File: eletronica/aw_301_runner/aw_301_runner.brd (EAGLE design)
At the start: 50.5 x 50.8 mm, 6 parts, among them IC1 ATTINY2313V

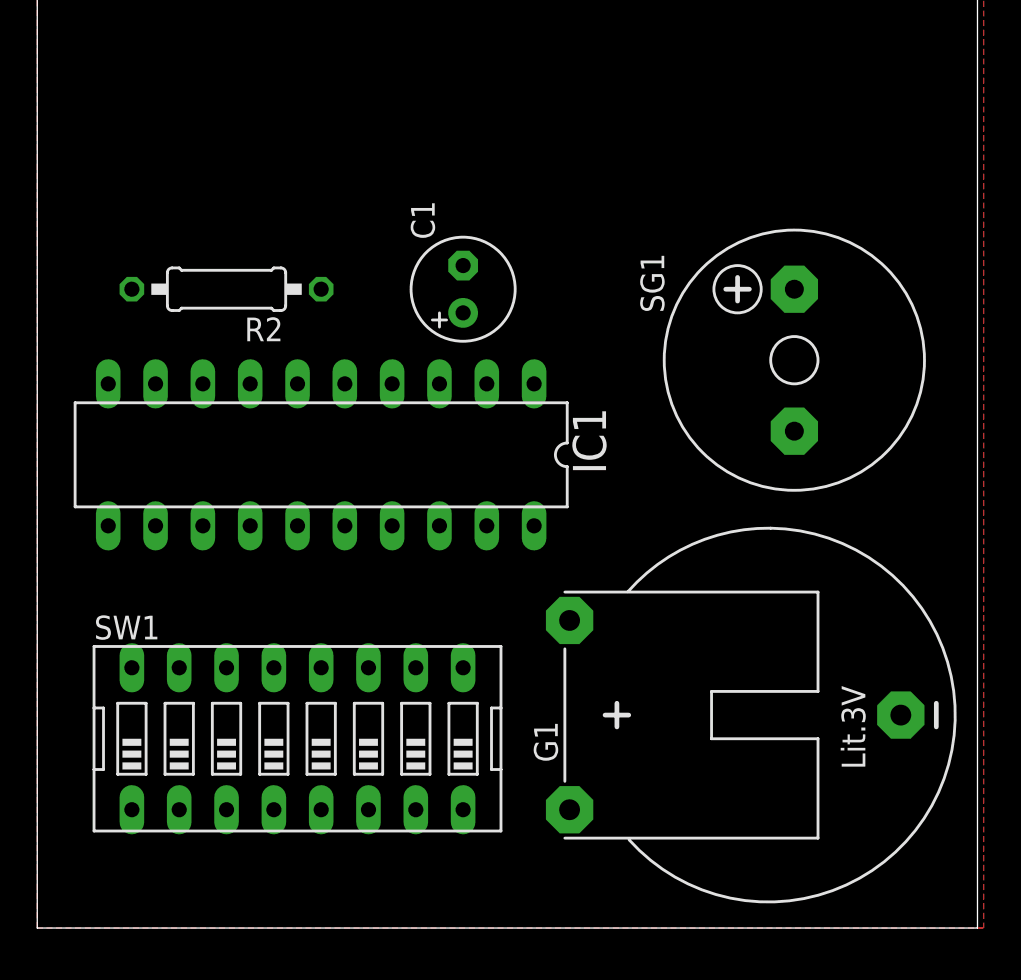
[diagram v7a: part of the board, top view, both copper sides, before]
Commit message: 
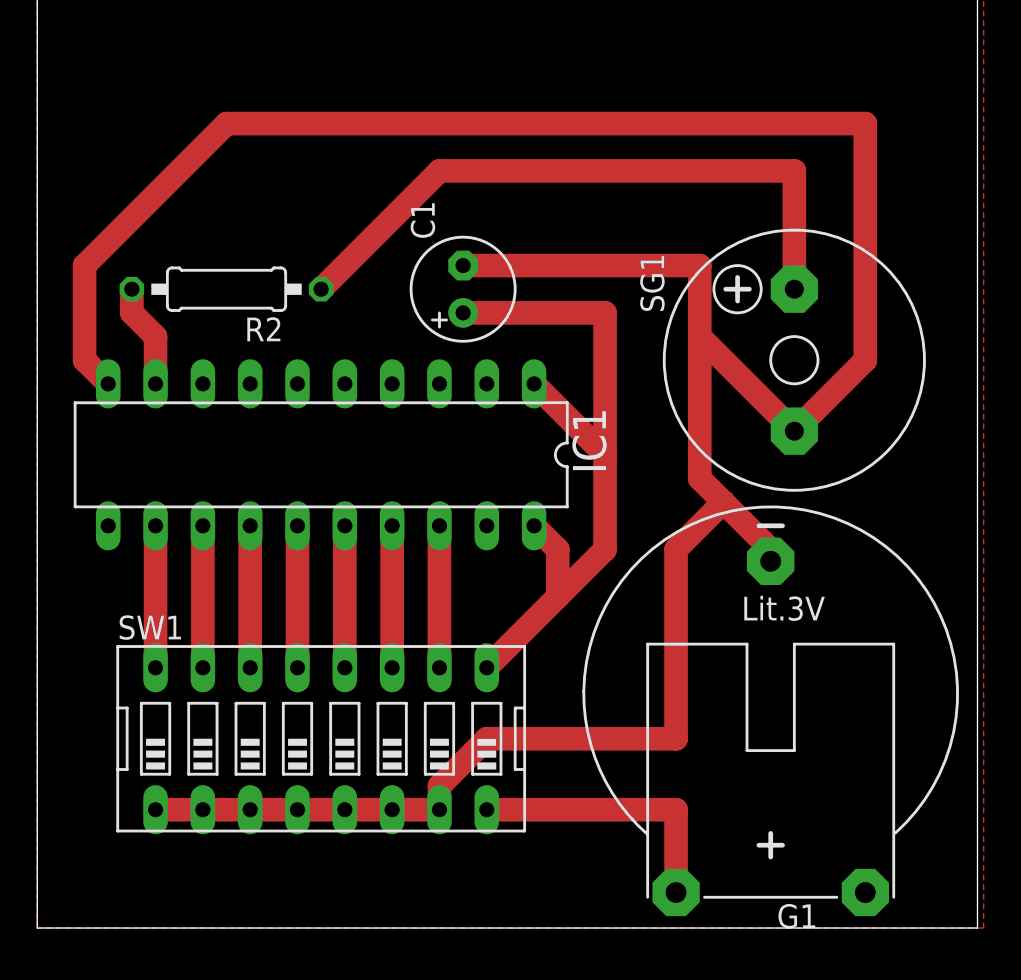
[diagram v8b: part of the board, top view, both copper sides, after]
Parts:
- moved G1 1.27 mm to (39.4, 12.7), turned to 180 degrees
- moved SW1 1.27 mm to (15.2, 10.2)
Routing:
- net GND: track 0.00 -> 151.4 mm
- net N$5: track 0.00 -> 39.0 mm
- net N$3: track 0.00 -> 34.4 mm
- net VCC: track 0.00 -> 14.6 mm
- net N$9: track 0.00 -> 7.62 mm
- net N$8: track 0.00 -> 7.62 mm
- net N$7: track 0.00 -> 7.62 mm
- net N$4: track 0.00 -> 7.62 mm
- net N$12: track 0.00 -> 7.62 mm
- net N$11: track 0.00 -> 7.62 mm
- net N$10: track 0.00 -> 7.62 mm
- net N$2: track 0.00 -> 5.61 mm
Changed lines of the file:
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@@
 <param name="PrefDir.14" value="0"/>
 <param name="PrefDir.15" value="0"/>
-<param name="PrefDir.16" value="-"/>
+<param name="PrefDir.16" value="0"/>
 <param name="cfVia" value="8"/>
 <param name="cfNonPref" value="5"/>
@@
 <attribute name="OC_FARNELL" value="unknown" x="-11.43" y="68.58" size="1.778" layer="27" rot="R180" display="off"/>
 </element>
-<element name="SW1" library="special" package="EDG-08" value="" x="13.97" y="10.16"/>
-<element name="G1" library="battery" package="CR2032H" value="CR2032H" x="39.37" y="11.43" rot="R90"/>
+<element name="SW1" library="special" package="EDG-08" value="" x="15.24" y="10.16"/>
+<element name="G1" library="battery" package="CR2032H" value="CR2032H" x="39.37" y="12.7" rot="R180"/>
 <element name="C1" library="resistor" package="E2,5-6" value="100mF" x="22.86" y="34.29" rot="R90"/>
 <element name="R2" library="rcl" package="0207/10" value="50" x="10.16" y="34.29" rot="R180"/>
@@
 <contactref element="SW1" pad="6"/>
 <contactref element="SW1" pad="7"/>
-<wire x1="20.32" y1="6.35" x2="46.355" y2="11.43" width="0" layer="19" extent="1-1"/>
-<wire x1="17.78" y1="6.35" x2="20.32" y2="6.35" width="0" layer="19" extent="1-1"/>
-<wire x1="15.24" y1="6.35" x2="17.78" y2="6.35" width="0" layer="19" extent="1-1"/>
-<wire x1="12.7" y1="6.35" x2="15.24" y2="6.35" width="0" layer="19" extent="1-1"/>
-<wire x1="10.16" y1="6.35" x2="12.7" y2="6.35" width="0" layer="19" extent="1-1"/>
-<wire x1="7.62" y1="6.35" x2="10.16" y2="6.35" width="0" layer="19" extent="1-1"/>
-<wire x1="5.08" y1="6.35" x2="7.62" y2="6.35" width="0" layer="19" extent="1-1"/>
-<wire x1="40.64" y1="26.67" x2="5.08" y2="6.35" width="0" layer="19" extent="1-1"/>
-<wire x1="3.81" y1="29.21" x2="5.08" y2="6.35" width="0" layer="19" extent="1-1"/>
-<wire x1="22.86" y1="35.56" x2="3.81" y2="29.21" width="0" layer="19" extent="1-1"/>
+<wire x1="8.89" y1="6.35" x2="6.35" y2="6.35" width="1.27" layer="1"/>
+<wire x1="8.89" y1="6.35" x2="11.43" y2="6.35" width="1.27" layer="1"/>
+<wire x1="11.43" y1="6.35" x2="13.97" y2="6.35" width="1.27" layer="1"/>
+<wire x1="13.97" y1="6.35" x2="16.51" y2="6.35" width="1.27" layer="1"/>
+<wire x1="16.51" y1="6.35" x2="19.05" y2="6.35" width="1.27" layer="1"/>
+<wire x1="19.05" y1="6.35" x2="21.59" y2="6.35" width="1.27" layer="1"/>
+<wire x1="2.54" y1="30.48" x2="3.81" y2="29.21" width="1.27" layer="1"/>
+<wire x1="2.54" y1="35.56" x2="2.54" y2="30.48" width="1.27" layer="1"/>
+<wire x1="10.16" y1="43.18" x2="2.54" y2="35.56" width="1.27" layer="1"/>
+<wire x1="44.45" y1="43.18" x2="10.16" y2="43.18" width="1.27" layer="1"/>
+<wire x1="44.45" y1="30.48" x2="44.45" y2="43.18" width="1.27" layer="1"/>
+<wire x1="40.64" y1="26.67" x2="44.45" y2="30.48" width="1.27" layer="1"/>
+<wire x1="35.56" y1="35.56" x2="22.86" y2="35.56" width="1.27" layer="1"/>
+<wire x1="35.56" y1="31.75" x2="35.56" y2="35.56" width="1.27" layer="1"/>
+<wire x1="40.64" y1="26.67" x2="35.56" y2="31.75" width="1.27" layer="1"/>
+<wire x1="35.56" y1="24.13" x2="36.83" y2="22.86" width="1.27" layer="1"/>
+<wire x1="36.83" y1="22.86" x2="39.37" y2="20.32" width="1.27" layer="1"/>
+<wire x1="35.56" y1="31.75" x2="35.56" y2="24.13" width="1.27" layer="1"/>
+<wire x1="39.37" y1="20.32" x2="39.37" y2="19.685" width="1.27" layer="1"/>
+<wire x1="21.59" y1="7.62" x2="21.59" y2="6.35" width="1.27" layer="1"/>
+<wire x1="24.13" y1="10.16" x2="21.59" y2="7.62" width="1.27" layer="1"/>
+<wire x1="34.29" y1="10.16" x2="24.13" y2="10.16" width="1.27" layer="1"/>
+<wire x1="34.29" y1="20.32" x2="34.29" y2="10.16" width="1.27" layer="1"/>
+<wire x1="36.83" y1="22.86" x2="34.29" y2="20.32" width="1.27" layer="1"/>
 </signal>
 <signal name="N$2">
 <contactref element="IC1" pad="9"/>
 <contactref element="R2" pad="2"/>
-<wire x1="6.35" y1="29.21" x2="5.08" y2="34.29" width="0" layer="19" extent="1-1"/>
+<wire x1="6.35" y1="31.75" x2="6.35" y2="29.21" width="1.27" layer="1"/>
+<wire x1="5.08" y1="33.02" x2="6.35" y2="31.75" width="1.27" layer="1"/>
+<wire x1="5.08" y1="34.29" x2="5.08" y2="33.02" width="1.27" layer="1"/>
 </signal>
 <signal name="N$6">
@@
 <contactref element="R2" pad="1"/>
 <contactref element="SG1" pad="+"/>
-<wire x1="40.64" y1="34.29" x2="15.24" y2="34.29" width="0" layer="19" extent="1-1"/>
+<wire x1="21.59" y1="40.64" x2="15.24" y2="34.29" width="1.27" layer="1"/>
+<wire x1="40.64" y1="40.64" x2="21.59" y2="40.64" width="1.27" layer="1"/>
+<wire x1="40.64" y1="34.29" x2="40.64" y2="40.64" width="1.27" layer="1"/>
 </signal>
 <signal name="VCC">
 <contactref element="G1" pad="+"/>
 <contactref element="SW1" pad="8"/>
-<wire x1="22.86" y1="6.35" x2="28.575" y2="16.51" width="0" layer="19" extent="1-1"/>
+<wire x1="34.29" y1="6.35" x2="24.13" y2="6.35" width="1.27" layer="1"/>
+<wire x1="34.29" y1="1.905" x2="34.29" y2="6.35" width="1.27" layer="1"/>
 </signal>
 <signal name="N$5">
@@
 <contactref element="C1" pad="+"/>
 <contactref element="IC1" pad="1"/>
-<wire x1="26.67" y1="21.59" x2="26.67" y2="29.21" width="0" layer="19" extent="1-1"/>
-<wire x1="22.86" y1="13.97" x2="26.67" y2="21.59" width="0" layer="19" extent="1-1"/>
-<wire x1="22.86" y1="33.02" x2="26.67" y2="29.21" width="0" layer="19" extent="1-1"/>
+<wire x1="27.94" y1="17.78" x2="24.13" y2="13.97" width="1.27" layer="1"/>
+<wire x1="27.94" y1="20.32" x2="27.94" y2="17.78" width="1.27" layer="1"/>
+<wire x1="26.67" y1="21.59" x2="27.94" y2="20.32" width="1.27" layer="1"/>
+<wire x1="30.48" y1="25.4" x2="26.67" y2="29.21" width="1.27" layer="1"/>
+<wire x1="30.48" y1="20.32" x2="30.48" y2="25.4" width="1.27" layer="1"/>
+<wire x1="27.94" y1="17.78" x2="30.48" y2="20.32" width="1.27" layer="1"/>
+<wire x1="30.48" y1="33.02" x2="22.86" y2="33.02" width="1.27" layer="1"/>
+<wire x1="30.48" y1="25.4" x2="30.48" y2="33.02" width="1.27" layer="1"/>
 </signal>
 <signal name="N$4">
 <contactref element="IC1" pad="12"/>
 <contactref element="SW1" pad="16"/>
-<wire x1="5.08" y1="13.97" x2="6.35" y2="21.59" width="0" layer="19" extent="1-1"/>
+<wire x1="6.35" y1="21.59" x2="6.35" y2="13.97" width="1.27" layer="1"/>
 </signal>
 <signal name="N$7">
 <contactref element="IC1" pad="13"/>
 <contactref element="SW1" pad="15"/>
-<wire x1="7.62" y1="13.97" x2="8.89" y2="21.59" width="0" layer="19" extent="1-1"/>
+<wire x1="8.89" y1="21.59" x2="8.89" y2="13.97" width="1.27" layer="1"/>
 </signal>
 <signal name="N$8">
 <contactref element="IC1" pad="14"/>
 <contactref element="SW1" pad="14"/>
-<wire x1="10.16" y1="13.97" x2="11.43" y2="21.59" width="0" layer="19" extent="1-1"/>
+<wire x1="11.43" y1="21.59" x2="11.43" y2="13.97" width="1.27" layer="1"/>
 </signal>
 <signal name="N$9">
 <contactref element="IC1" pad="15"/>
 <contactref element="SW1" pad="13"/>
-<wire x1="12.7" y1="13.97" x2="13.97" y2="21.59" width="0" layer="19" extent="1-1"/>
+<wire x1="13.97" y1="21.59" x2="13.97" y2="13.97" width="1.27" layer="1"/>
 </signal>
 <signal name="N$10">
 <contactref element="IC1" pad="16"/>
 <contactref element="SW1" pad="12"/>
-<wire x1="15.24" y1="13.97" x2="16.51" y2="21.59" width="0" layer="19" extent="1-1"/>
+<wire x1="16.51" y1="21.59" x2="16.51" y2="13.97" width="1.27" layer="1"/>
 </signal>
 <signal name="N$11">
 <contactref element="IC1" pad="17"/>
 <contactref element="SW1" pad="11"/>
-<wire x1="17.78" y1="13.97" x2="19.05" y2="21.59" width="0" layer="19" extent="1-1"/>
+<wire x1="19.05" y1="21.59" x2="19.05" y2="13.97" width="1.27" layer="1"/>
 </signal>
 <signal name="N$12">
 <contactref element="IC1" pad="18"/>
 <contactref element="SW1" pad="10"/>
-<wire x1="20.32" y1="13.97" x2="21.59" y2="21.59" width="0" layer="19" extent="1-1"/>
+<wire x1="21.59" y1="21.59" x2="21.59" y2="13.97" width="1.27" layer="1"/>
 </signal>
 </signals>
